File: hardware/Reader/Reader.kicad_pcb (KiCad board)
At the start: 2 copper layers, 120 parts, among them IC3 MCP2562-H_MF, IC5 MCP2562-H_MF, IC6 TH8056KDC-AAA-014-RE, IC7 LM339N_NOPB, IC8 LM317LDR2G, X1 ECS-2033-160-AU (16MHz)

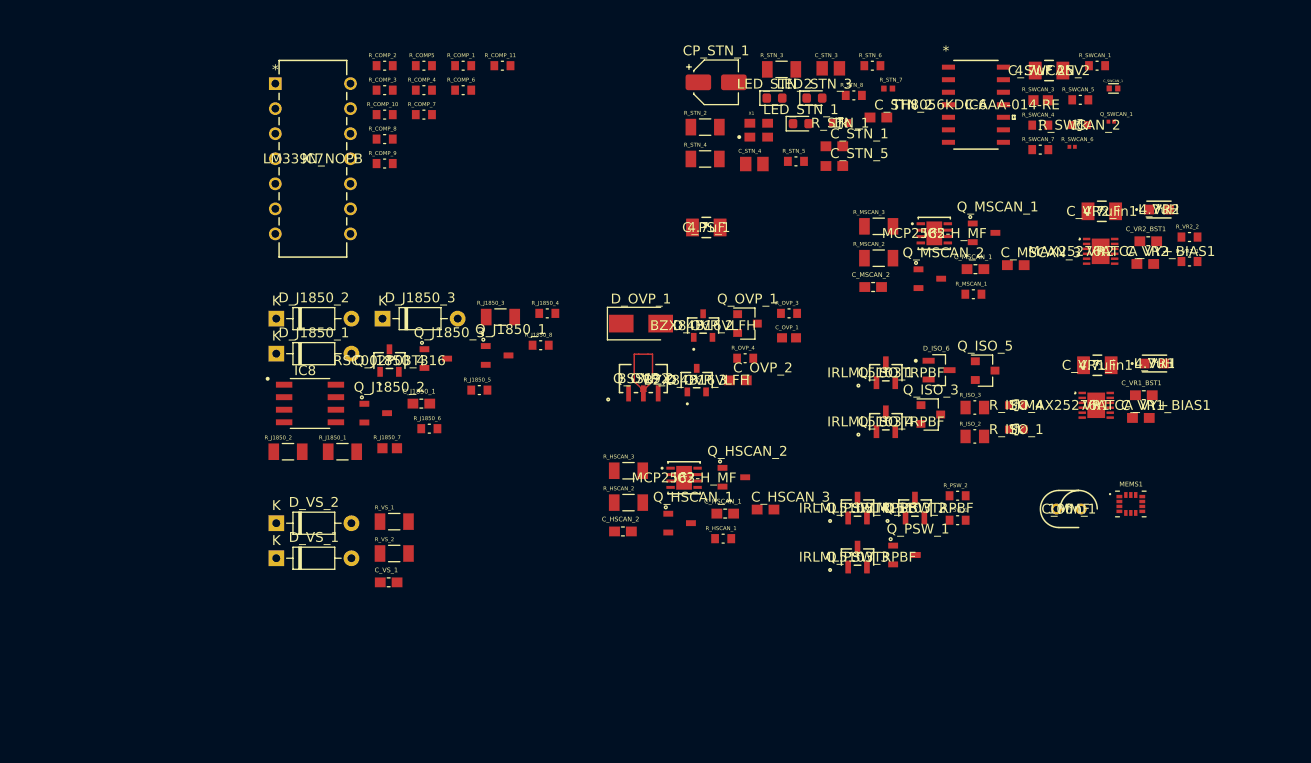
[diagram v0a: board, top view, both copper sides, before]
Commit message: Completed Reader schematics for version 0.0.01
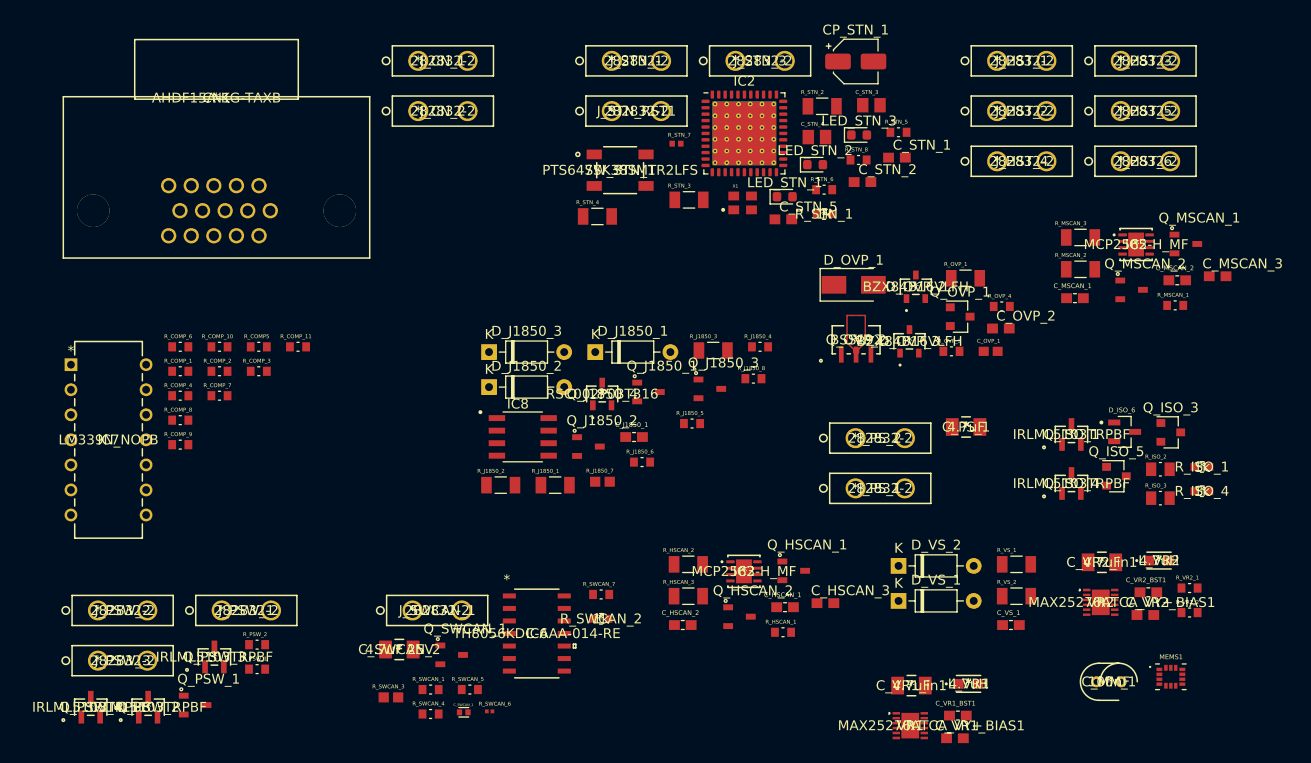
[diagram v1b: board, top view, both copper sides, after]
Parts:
- added CN1: AHDF15A-KG-TAXB, footprints:AHDF15A-KG-TAXB, F.Cu at (98.3, 41.7)
- added IC2: STN2120, Package_DFN_QFN:QFN-44-1EP_8x8mm_P0.65mm_EP6.45x6.45mm_ThermalVias, F.Cu at (151.8, 45.3)
- added J_CN_1: 282832-2, footprints:282832-2, F.Cu at (118.7, 37.9)
- added J_CN_2: 282832-2, footprints:282832-2, F.Cu at (118.7, 43.0)
- added J_HST_1: 282832-2, footprints:282832-2, F.Cu at (177.4, 37.9)
- added J_HST_2: 282832-2, footprints:282832-2, F.Cu at (177.4, 43.0)
- added J_HST_3: 282832-2, footprints:282832-2, F.Cu at (190.0, 37.9)
- added J_HST_4: 282832-2, footprints:282832-2, F.Cu at (177.4, 48.1)
- added J_HST_5: 282832-2, footprints:282832-2, F.Cu at (190.0, 43.0)
- added J_HST_6: 282832-2, footprints:282832-2, F.Cu at (190.0, 48.1)
- added J_PSW_1: 282832-2, footprints:282832-2, F.Cu at (98.8, 93.6)
- added J_PSW_2: 282832-2, footprints:282832-2, F.Cu at (86.3, 93.6)
- added J_PSW_3: 282832-2, footprints:282832-2, F.Cu at (86.3, 98.7)
- added J_PS_1: 282832-2, footprints:282832-2, F.Cu at (163.1, 81.3)
- added J_PS_2: 282832-2, footprints:282832-2, F.Cu at (163.1, 76.2)
- added J_STN_1: 282832-2, footprints:282832-2, F.Cu at (138.4, 37.9)
- added J_STN_3: 282832-2, footprints:282832-2, F.Cu at (150.9, 37.9)
- added J_STN_RST1: 282832-2, footprints:282832-2, F.Cu at (138.4, 43.0)
- added J_SWCAN_1: 282832-2, footprints:282832-2, F.Cu at (118.2, 93.6)
- added R_OVP_1: 100, footprints:RESC3216X70N, F.Cu at (174.2, 60.0)
- added SW_STN_1: PTS647SK38SMTR2LFS, footprints:PTS647SK38SMTR2LFS, F.Cu at (139.2, 49.0)
- Q_SWCAN_1: footprint footprints:RESC0603X26N -> footprints:SOT95P230X110-3N
- moved R_SWCAN_1 92.6 mm to (120.0, 101.7)
- moved C_SWCAN_1 91.3 mm to (123.4, 104.0)
- moved R_SWCAN_3 89.5 mm to (116.0, 102.5)
- moved C_SWCAN_2 88.2 mm to (116.8, 97.6)
- moved R_SWCAN_5 86.1 mm to (124.0, 101.7)
- moved Q_SWCAN_1 86.0 mm to (122.1, 98.1)
- moved R_SWCAN_4 85.9 mm to (120.0, 104.1)
- moved R_SWCAN_6 82.2 mm to (126.0, 103.9)
- moved Q_PSW_2 80.3 mm to (91.4, 103.4)
- moved Q_PSW_4 80.3 mm to (85.5, 103.4)
- moved Q_PSW_1 73.5 mm to (96.1, 103.2)
- moved R_PSW_1 72.6 mm to (102.4, 99.6)
- moved R_PSW_2 72.6 mm to (102.4, 97.1)
- moved R_SWCAN_2 69.7 mm to (137.3, 94.5)
- moved IC6 69.7 mm to (130.8, 96.0)
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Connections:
- net Net-(MEMS1-Pad1) renamed /Host/MEMS_SA0
- net Net-(MEMS1-Pad9) renamed /Reader MEMs/MEMS_INT2
- C_MM_1 pad 1: Pin4_GnD_Chassis -> +3.3V_SW
- D_J1850_1 pad 2: Pin4_GnD_Chassis -> +5V_SW
- IC7 pad 3: +12V -> +12V_SW
- MEMS1 pad 12: Net-(MEMS1-Pad12) -> /Host/MEMS_CS
- MEMS1 pad 13: /Reader MEMs/MEMS_SCL -> /Host/I2C_SCL
- MEMS1 pad 14: /Reader MEMs/MEMS_SDA -> /Host/I2C_SDA
- MEMS1 pad 4: /Reader MEMs/MEMS_INT -> /Host/MEMS_INT
- MEMS1 pad 5: Pin4_GnD_Chassis -> +3.3V_SW
- MEMS1 pad 8: Pin4_GnD_Chassis -> +3.3V_SW
- Q_ISO_1 pad 1: /OBDII Interpreter/ISO 9141/ISO 14230 Transceiver/PWR_CTRL -> /OBDII Interpreter/PWR_CTRL
- Q_ISO_4 pad 1: /OBDII Interpreter/ISO 9141/ISO 14230 Transceiver/PWR_CTRL -> /OBDII Interpreter/PWR_CTRL
- Q_PSW_1 pad 1: Net-(Q_PSW_1-Pad1) -> /OBDII Interpreter/~PWR_CTRL~
- Q_PSW_1 pad 3: Net-(Q_PSW_1-Pad3) -> /OBDII Interpreter/PWR_CTRL
- Q_PSW_2 pad 1: Net-(Q_PSW_1-Pad3) -> /OBDII Interpreter/PWR_CTRL
- Q_PSW_2 pad 2: +12V -> +12V_SW
- Q_PSW_3 pad 1: Net-(Q_PSW_1-Pad3) -> /OBDII Interpreter/PWR_CTRL
- Q_PSW_3 pad 2: Pin4_GnD_Chassis -> +5V_SW
- Q_PSW_4 pad 1: Net-(Q_PSW_1-Pad3) -> /OBDII Interpreter/PWR_CTRL
- Q_PSW_4 pad 2: Pin4_GnD_Chassis -> +3.3V_SW
- R_COMP_6 pad 1: +12V -> +12V_SW
- R_COMP_8 pad 1: Pin4_GnD_Chassis -> +5V_SW
- R_PSW_1 pad 2: Net-(Q_PSW_1-Pad1) -> /OBDII Interpreter/~PWR_CTRL~
- R_PSW_2 pad 2: Net-(Q_PSW_1-Pad3) -> /OBDII Interpreter/PWR_CTRL
- R_STN_1 pad 2: /OBDII Interpreter/STN2110_RX -> /Host/HOST_TX
- R_STN_8 pad 2: /OBDII Interpreter/~SLEEP_OBD~ -> /Host/~RESET_OBD_HW~
- R_SWCAN_4 pad 1: Pin4_GnD_Chassis -> +5V_SW
- R_SWCAN_5 pad 1: Pin4_GnD_Chassis -> +5V_SW

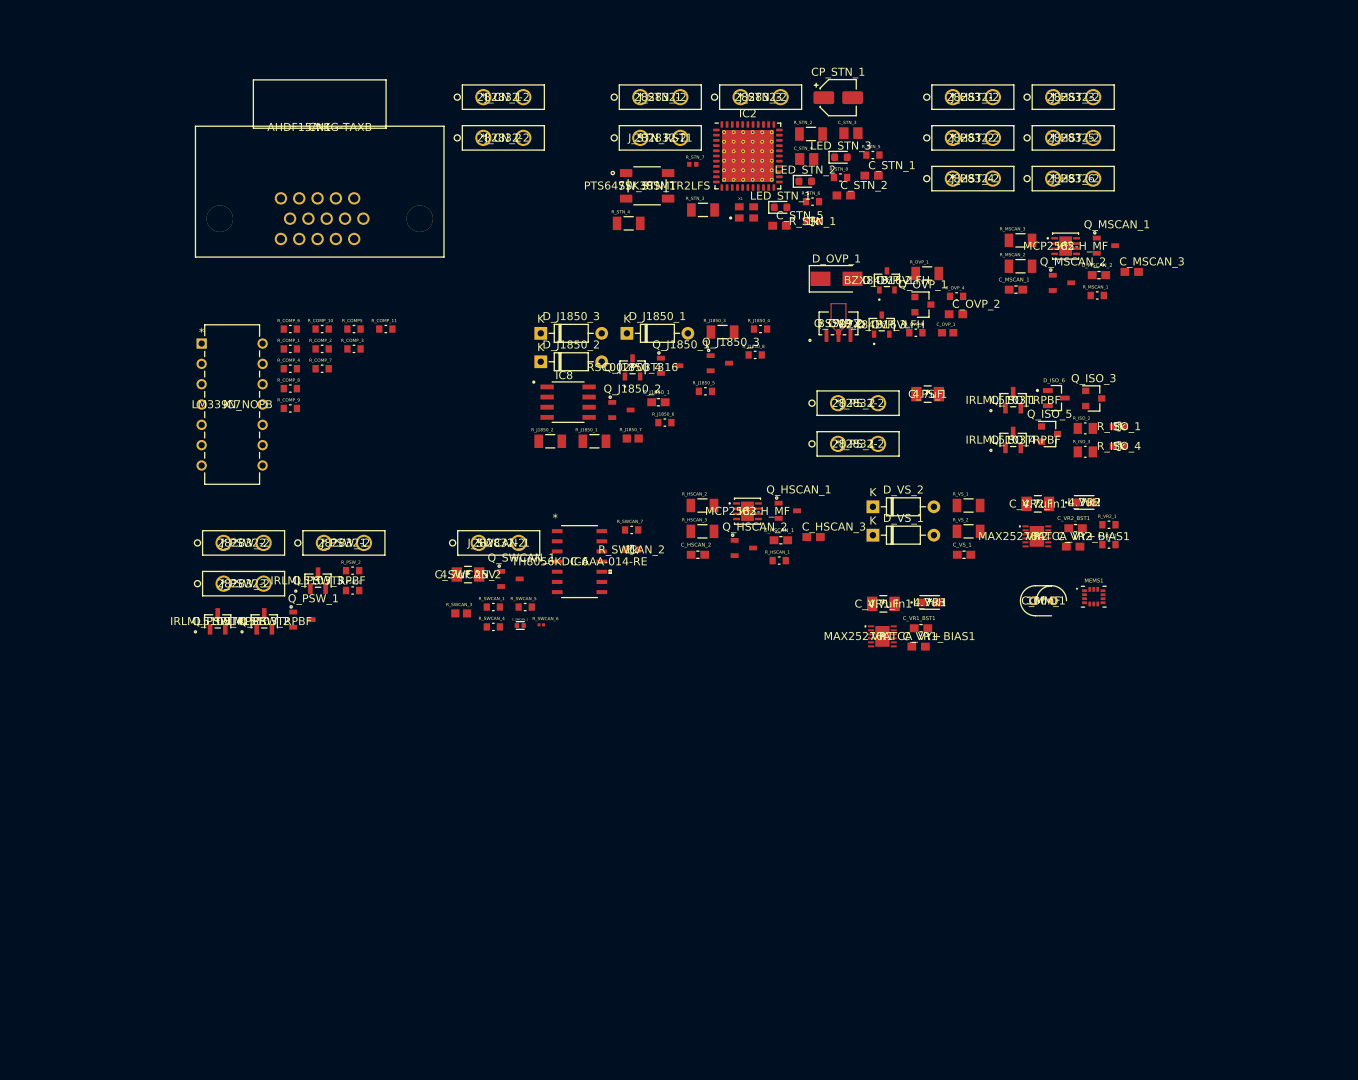
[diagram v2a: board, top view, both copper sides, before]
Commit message: Added ESD Protection. Fixed minor bugs on schematic. Attempted placement of components
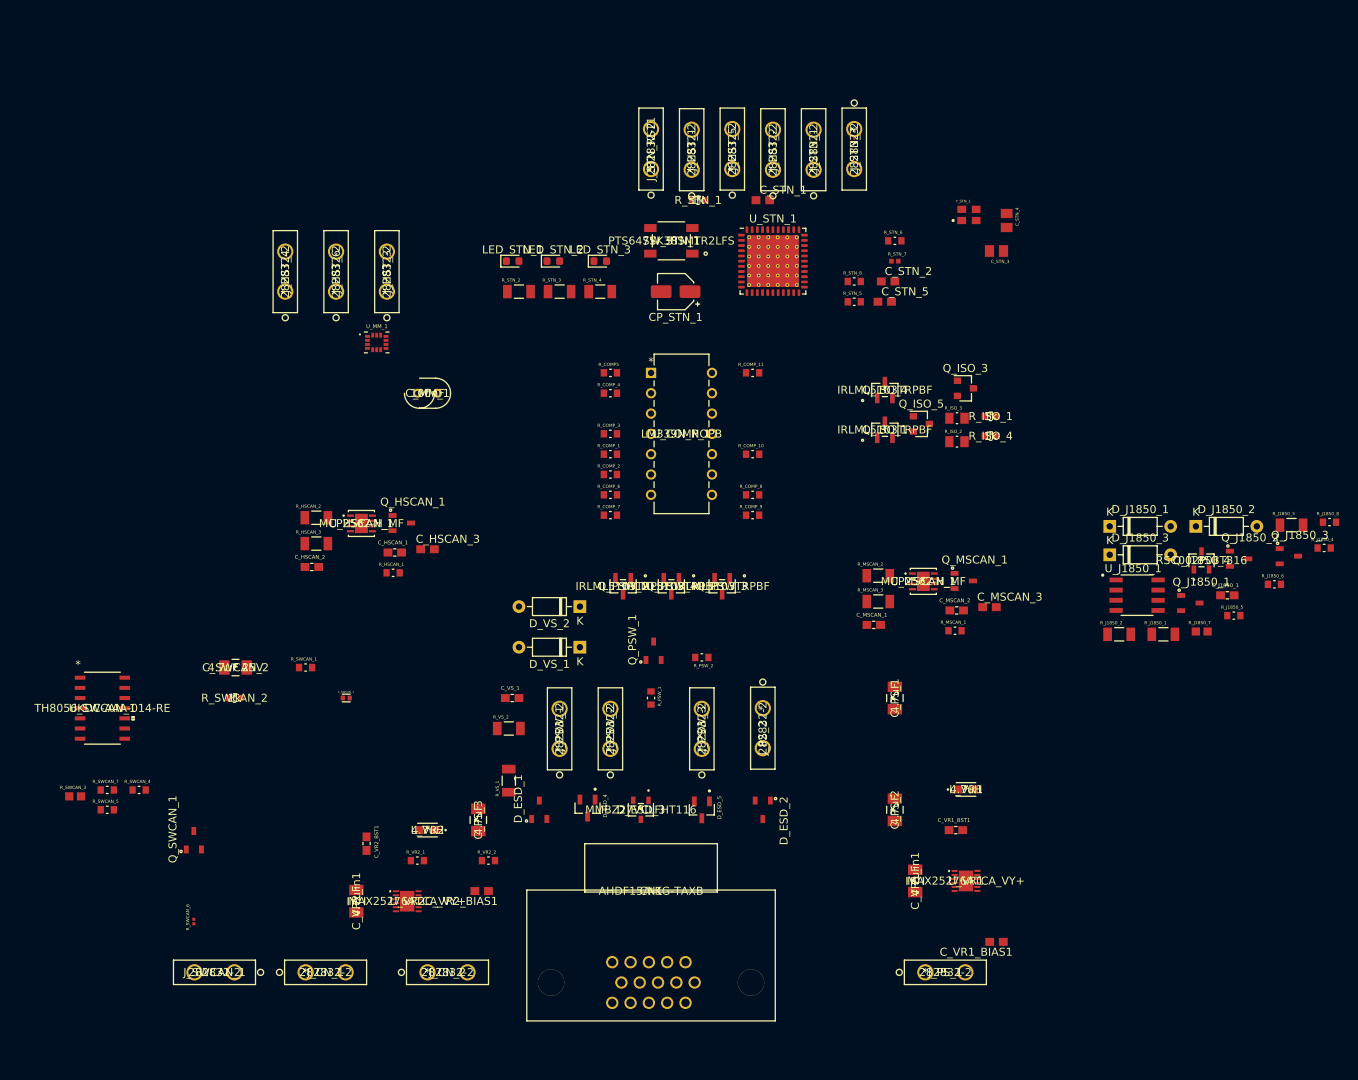
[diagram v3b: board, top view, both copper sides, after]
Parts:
- removed C_OVP_1: 10nF/100V, footprints:CAPC1608X90N
- removed C_OVP_2: 1uF, footprints:0603
- removed D_ISO_6: MMBZ27VALT3G, SOT95P237X111-3N
- removed D_OVP_1: US2AA, Diode_SMD:D_SMA
- removed D_OVP_2, D_OVP_3: BZX84B16VLFH, footprints:BZX84B16VLFHT116
- removed IC2: STN2120, Package_DFN_QFN:QFN-44-1EP_8x8mm_P0.65mm_EP6.45x6.45mm_ThermalVias
- removed IC3, IC5: MCP2562-H_MF, footprints:MCP2562-H&slash_MF
- removed IC6: TH8056KDC-AAA-014-RE, footprints:TH8056KDC-AAA-014-RE
- removed IC7: LM339N_NOPB, footprints:LM339N&slash_NOPB
- removed IC8: LM317LDR2G, footprints:SOIC127P600X175-8N
- removed MEMS1: LSM6DSMTR, footprints:PQFN50P300X250X86-14N
- removed Q_HSCAN_2, Q_MSCAN_2: PESD2CAN,215, footprints:SOT95P230X110-3N
- removed Q_OVP_1: MMBT3906, Package_TO_SOT_SMD:SOT-23
- removed Q_OVP_2: BSS192, footprints:BSS192
- removed R_OVP_1: 100, footprints:RESC3216X70N
- removed R_OVP_3: 10k, footprints:RESC1608X55N
- removed R_OVP_4: 100k, footprints:RESC1608X55N
- removed VR1, VR2: MAX25276ATCA_VY+, footprints:MAX25276ATCA&slash_VY&plus_
- removed X1: ECS-2033-160-AU (16MHz), footprints:OSC_ECS-2033-160-AU
- added C_PS_2: 4.7uF, footprints:C1206C475K3RACAUTO, F.Cu at (170.2, 127.0)
- added C_PS_3: 4.7uF, footprints:C1206C475K3RACAUTO, F.Cu at (118.1, 128.3)
- added D_ESD_1: PESD2CAN,215, footprints:SOT95P230X110-3N, F.Cu at (125.7, 127.0)
- added D_ESD_2: PESD2CAN,215, footprints:SOT95P230X110-3N, F.Cu at (153.7, 127.0)
- added D_ESD_3: MMBZ27VCLFHT116, footprints:MMBZ27VCLFHT116, F.Cu at (138.4, 127.0)
- added D_ESD_4: MMBZ27VALT3G, footprints:SOT95P237X111-3N, F.Cu at (131.8, 126.8)
- added D_ESD_5: MMBZ27VALT3G, footprints:SOT95P237X111-3N, F.Cu at (146.1, 127.0)
- added U_COMP_1: LM339N_NOPB, footprints:LM339N&slash_NOPB, F.Cu at (139.7, 72.4)
- added U_HSCAN_1: MCP2562-H_MF, footprints:MCP2562-H&slash_MF, F.Cu at (103.5, 91.2)
- added U_J1850_1: LM317LDR2G, footprints:SOIC127P600X175-8N, F.Cu at (200.5, 100.2)
- added U_MM_1: LSM6DSMTR, footprints:PQFN50P300X250X86-14N, F.Cu at (105.4, 68.6)
- added U_MSCAN_1: MCP2562-H_MF, footprints:MCP2562-H&slash_MF, F.Cu at (173.7, 98.4)
- added U_STN_1: STN2120, Package_DFN_QFN:QFN-44-1EP_8x8mm_P0.65mm_EP6.45x6.45mm_ThermalVias, F.Cu at (154.9, 58.4)
- added U_SWCAN_1: TH8056KDC-AAA-014-RE, footprints:TH8056KDC-AAA-014-RE, F.Cu at (71.1, 114.3)
- added U_VR1: MAX25276ATCA_VY+, footprints:MAX25276ATCA&slash_VY&plus_, F.Cu at (179.1, 135.9)
- added U_VR2: MAX25276ATCA_VY+, footprints:MAX25276ATCA&slash_VY&plus_, F.Cu at (109.2, 138.4)
- added Y_STN_1: ECS-2033-160-AU (16MHz), footprints:OSC_ECS-2033-160-AU, F.Cu at (179.4, 52.6)
- moved J_CN_1 111.6 mm to (96.5, 147.3)
- moved J_CN_2 104.5 mm to (111.8, 147.3)
- moved CN1 104.1 mm to (139.7, 137.2)
- moved C_VR2_in1 98.6 mm to (102.9, 138.4), turned to 90 degrees
- moved C_VR2_BST1 97.0 mm to (104.1, 131.2), turned to 270 degrees
- moved R_VR2_1 96.1 mm to (110.5, 133.3)
- moved L_VR2 91.7 mm to (111.8, 129.5), turned to 180 degrees
- moved J_HST_6 90.7 mm to (100.3, 62.2), turned to 90 degrees
- moved R_VR2_2 87.0 mm to (119.4, 133.3)
- moved J_HST_3 86.8 mm to (106.7, 62.2), turned to 90 degrees
- moved C_VR2_BIAS1 85.6 mm to (118.5, 137.2), turned to 180 degrees
- moved J_HST_4 84.6 mm to (94.0, 62.2), turned to 90 degrees
- moved D_J1850_2 84.4 mm to (207.8, 91.6)
- moved C_MM_1 81.2 mm to (111.8, 74.9), turned to 180 degrees
- moved Q_J1850_2 79.4 mm to (213.2, 95.6)
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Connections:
- CN1 pad 11: Pin6_ISO15765-4_CAN_BUS_High -> Pin14_ISO15765-4_CAN_BUS_Low
- CN1 pad 6: Pin7_ISO9141_K-Line -> Pin15_ISO9141_L-Line
- C_HSCAN_3 pad 2: Pin4_GnD_Chassis -> +5V
- C_MSCAN_3 pad 2: Pin4_GnD_Chassis -> +5V
- C_STN_1 pad 1: Pin4_GnD_Chassis -> +3V3
- C_STN_2 pad 1: Pin4_GnD_Chassis -> +3V3
- C_VR2_in1 pad 2: Pin4_GnD_Chassis -> +12V
- D_VS_1 pad 1: Pin4_GnD_Chassis -> +3V3
- J_CN_1 pad 1: Pin6_ISO15765-4_CAN_BUS_High -> Pin14_ISO15765-4_CAN_BUS_Low
- J_CN_2 pad 1: Pin7_ISO9141_K-Line -> Pin15_ISO9141_L-Line
- J_HST_5 pad 1: Pin4_GnD_Chassis -> +5V
- J_PSW_2 pad 2: Pin4_GnD_Chassis -> +5V
- J_PSW_3 pad 2: Pin4_GnD_Chassis -> +3V3
- J_PS_2 pad 1: Pin4_GnD_Chassis -> +5V
- J_PS_2 pad 2: Pin4_GnD_Chassis -> +3V3
- LED_STN_1 pad 2: Pin4_GnD_Chassis -> +3V3
- LED_STN_2 pad 2: Pin4_GnD_Chassis -> +3V3
- LED_STN_3 pad 2: Pin4_GnD_Chassis -> +3V3
- L_VR1 pad 1: Pin4_GnD_Chassis -> +5V
- L_VR2 pad 1: Pin4_GnD_Chassis -> +3V3
- Q_ISO_3 pad 3: Pin7_ISO9141_K-Line -> Pin15_ISO9141_L-Line
- Q_J1850_2 pad 3: Pin10_SAE_J1850_BUS- -> /OBDII Interpreter/J1850_BUS-
- Q_PSW_3 pad 3: Pin4_GnD_Chassis -> +5V
- Q_PSW_4 pad 3: Pin4_GnD_Chassis -> +3V3
- R_COMP5 pad 1: Pin4_GnD_Chassis -> +3V3
- R_COMP_11 pad 1: Pin4_GnD_Chassis -> +3V3
- R_COMP_2 pad 1: Pin7_ISO9141_K-Line -> Pin15_ISO9141_L-Line
- R_COMP_3 pad 2: Pin10_SAE_J1850_BUS- -> /OBDII Interpreter/J1850_BUS-
- R_COMP_4 pad 1: Pin4_GnD_Chassis -> +3V3
- R_HSCAN_1 pad 1: Pin4_GnD_Chassis -> +3V3
- R_HSCAN_3 pad 1: Pin6_ISO15765-4_CAN_BUS_High -> Pin14_ISO15765-4_CAN_BUS_Low
- R_ISO_2 pad 1: Pin7_ISO9141_K-Line -> Pin15_ISO9141_L-Line
- R_J1850_5 pad 2: Pin10_SAE_J1850_BUS- -> /OBDII Interpreter/J1850_BUS-
- R_MSCAN_1 pad 1: Pin4_GnD_Chassis -> +3V3
- R_PSW_1 pad 1: Pin4_GnD_Chassis -> +3V3
- R_STN_1 pad 1: Pin4_GnD_Chassis -> +3V3
- R_STN_5 pad 2: Pin4_GnD_Chassis -> +3V3
- R_STN_6 pad 1: Pin4_GnD_Chassis -> +3V3
- R_STN_7 pad 1: Pin4_GnD_Chassis -> +3V3
- R_STN_8 pad 1: Pin4_GnD_Chassis -> +3V3
- R_SWCAN_2 pad 2: Pin4_GnD_Chassis -> +3V3
- R_SWCAN_3 pad 2: Pin4_GnD_Chassis -> +5V
- R_VR2_2 pad 1: Pin4_GnD_Chassis -> +3V3
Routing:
- net /OBDII Interpreter/~PWR_CTRL~: track 0.00 -> 1.27 mm
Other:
- copper layers 2 -> 4
- rule via_min_drill: 0.3 -> 0.305
